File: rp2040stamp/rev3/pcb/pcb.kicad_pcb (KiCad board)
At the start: 2 copper layers, 24 x 19.5 mm, 26 parts, among them U1 RP2040, U2 Memory_Flash_W25Q64_XSON, U3 NCP114ASN330T1G, X1 12.000MHz

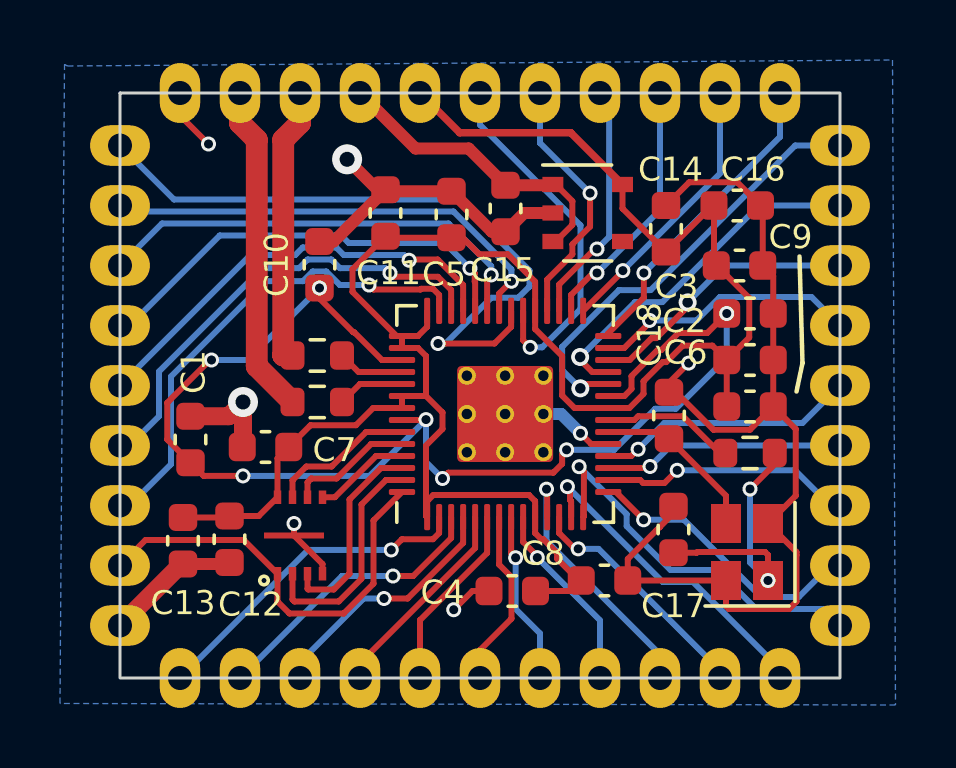
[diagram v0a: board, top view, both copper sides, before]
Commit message: M  giri-kicad-lib/switches_lib.pretty/Gateron_1.25u_v2.kicad_mod M  giri-kicad-lib/switches_lib.pretty/Gateron_1u_v2.kicad_mod M  giri-kicad-lib/switches_lib.pretty/Gateron_2u_v2.kicad_mod A  giri-kicad-lib/switches_lib.pretty/SMTSO_M2_FrontPad_M2_hole.kicad_mod A  giri-kicad-lib/switches_lib.pretty/Switch_Cutout2_MX.kicad_mod A  giri-kicad-lib/switches_lib.pretty/Switch_Cutout2_MX_1.25u.kicad_mod A  giri-kicad-lib/switches_lib.pretty/Switch_Cutout2_MX_2u.kicad_mod M  mx/rev3/bottom-cover/pcb/pcb.kicad_pcb M  mx/rev3/bottom-cover/pcb/pcb.kicad_prl M  mx/rev3/bottom-cover/pcb/pcb.kicad_sch M  mx/rev3/pcb-rev2/pcb/pcb.kicad_pcb M  mx/rev3/pcb-rev2/pcb/pcb.kicad_prl M  mx/rev3/pcb-rev2/pcb/pcb.kicad_sch M  mx/rev3/switch-plate-wide/fp-lib-table M  mx/rev3/switch-plate-wide/switch-plate-wide.kicad_pcb M  mx/rev3/switch-plate-wide/switch-plate-wide.kicad_sch A  mx/rev4/notes D  nrfStamp/rev1/pcb/~pcb.kicad_sch.lck D  rp2040stamp/rev2/pcb/~pcb.kicad_sch.lck M  rp2040stamp/rev3/pcb/fp-lib-table M  rp2040stamp/rev3/pcb/pcb.kicad_pcb M  rp2040stamp/rev3/pcb/pcb.kicad_prl M  rp2040stamp/rev3/pcb/pcb.kicad_sch M  rp2040stamp/rev3/pcb/sym-lib-table
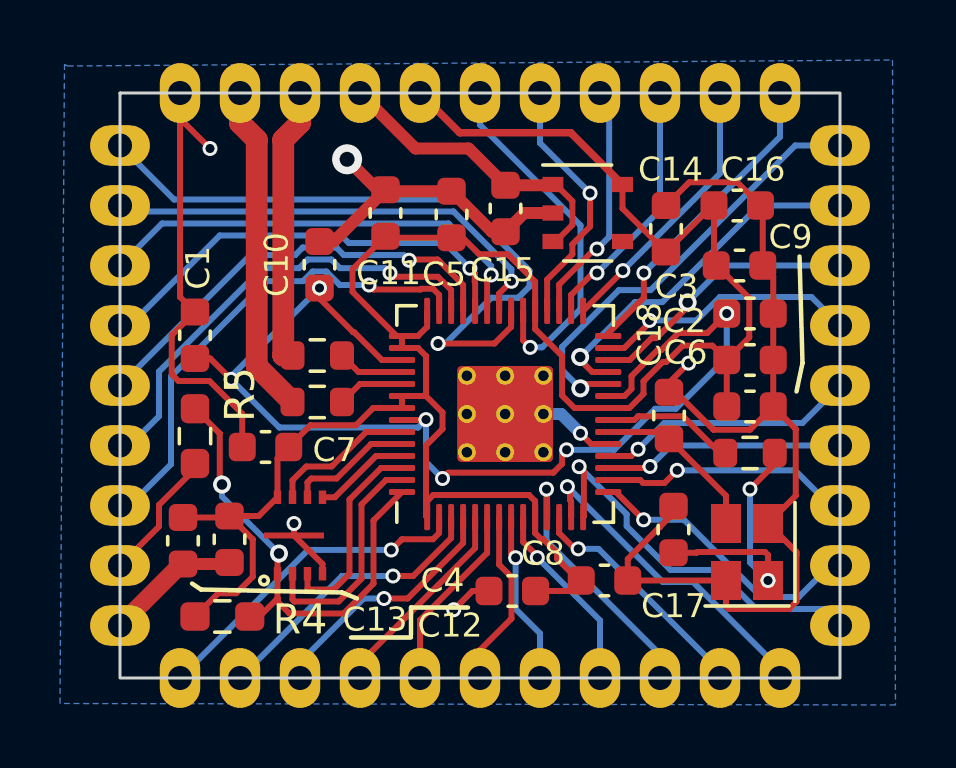
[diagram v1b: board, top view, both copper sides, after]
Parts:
- added R4: 10k, RP2040_Minimal:R_0603_1608Metric_Pad0.98x0.95mm_HandSolder, F.Cu at (101.7, 101.5)
- added R5: 1k, RP2040_Minimal:R_0603_1608Metric_Pad0.98x0.95mm_HandSolder, F.Cu at (100.8, 95.5)
- moved C1 3.48 mm to (100.8, 92.1)
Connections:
- ST1 pad 8: /QSPI_SS -> /~{USB_BOOT}
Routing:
- net GND: track 61.0 -> 71.7 mm, vias 7 -> 6
- net +3V3: track 70.7 -> 75.5 mm
- net +1V1: track 42.9 -> 38.1 mm, vias 7 -> 6
- net /~{USB_BOOT}: track 0.00 -> 4.44 mm
- net /QSPI_SS: track 14.2 -> 16.0 mm, vias 0 -> 2
